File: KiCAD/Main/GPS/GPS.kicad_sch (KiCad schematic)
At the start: 17 parts, among them U1 MAX-M8Q, U2 PHA-23LN

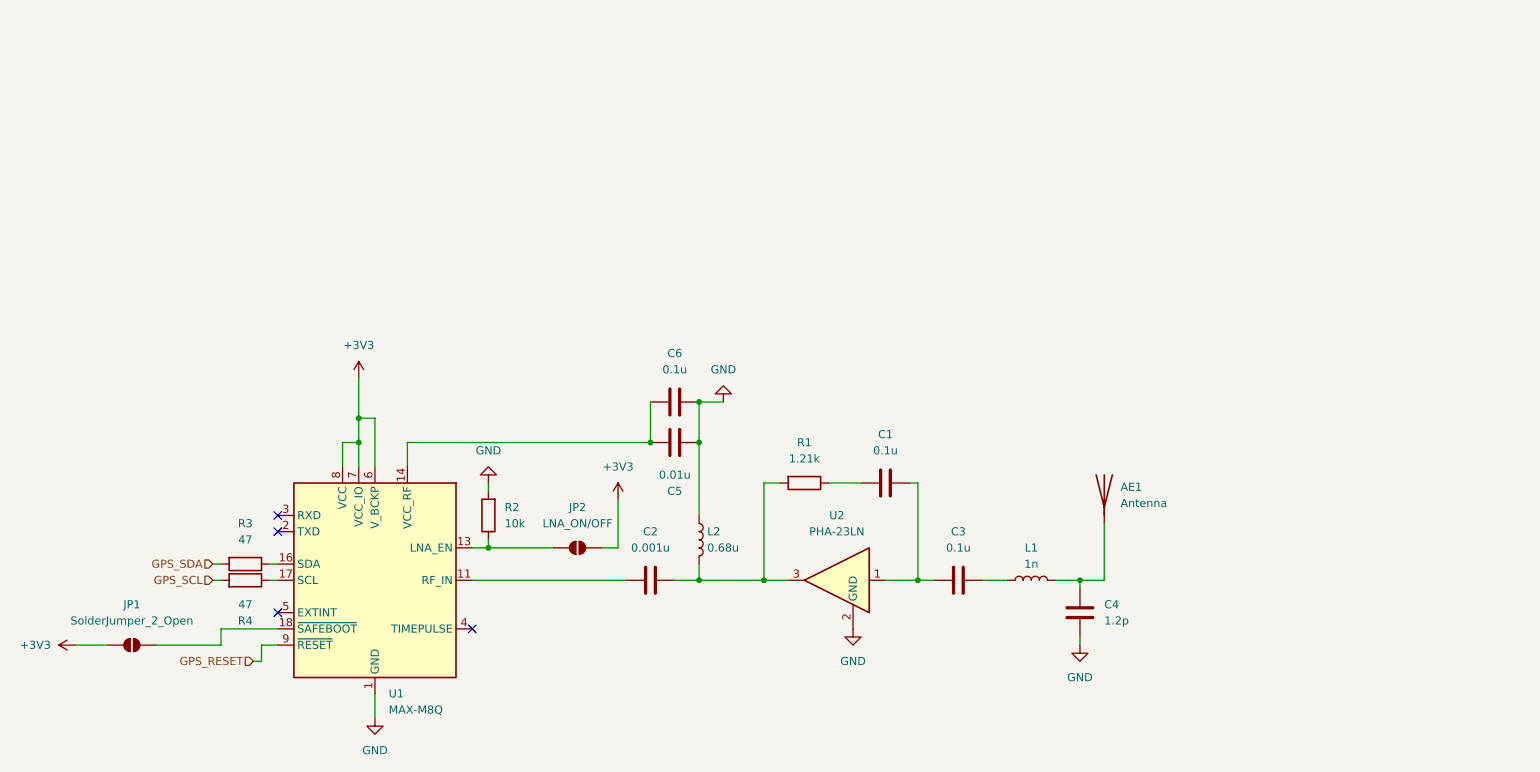
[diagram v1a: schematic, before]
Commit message: Create wiring diagram draft
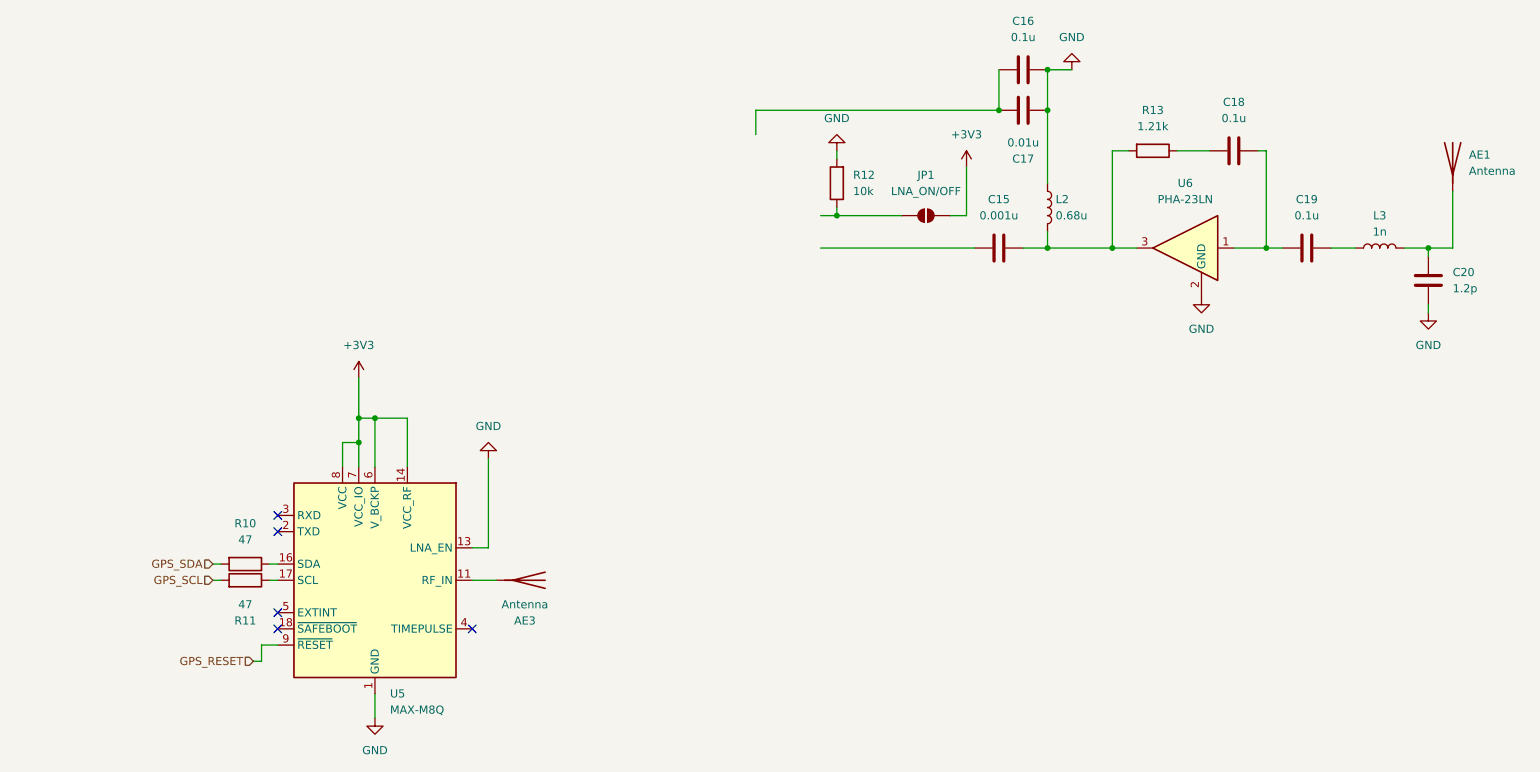
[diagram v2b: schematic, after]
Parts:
- removed JP1: SolderJumper_2_Open, symbol Jumper:SolderJumper_2_Open
- added AE3: Antenna, symbol Device:Antenna
- renumbered C2 to C15, C6 to C16, C5 to C17, C1 to C18, C3 to C19, C4 to C20, JP2 to JP1, L1 to L3, R3 to R10, R4 to R11, R2 to R12, R1 to R13, U1 to U5, U2 to U6
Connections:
- net +3V3: now also U5.14 (VCC_RF)
- net GND: now also U5.13 (LNA_EN)
- net at U5.11 (RF_IN): now also AE3.1 (A); no longer C15.1
- net at JP1.1 (A), R12.1: no longer U5.13 (LNA_EN)
- net at C16.2, C17.2: no longer U5.14 (VCC_RF)
- no-connect marks 4 -> 5
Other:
- moved on the sheet: AE1, C15, C16, C17, C18, C19, C20, JP1, L2, L3, R12, R13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

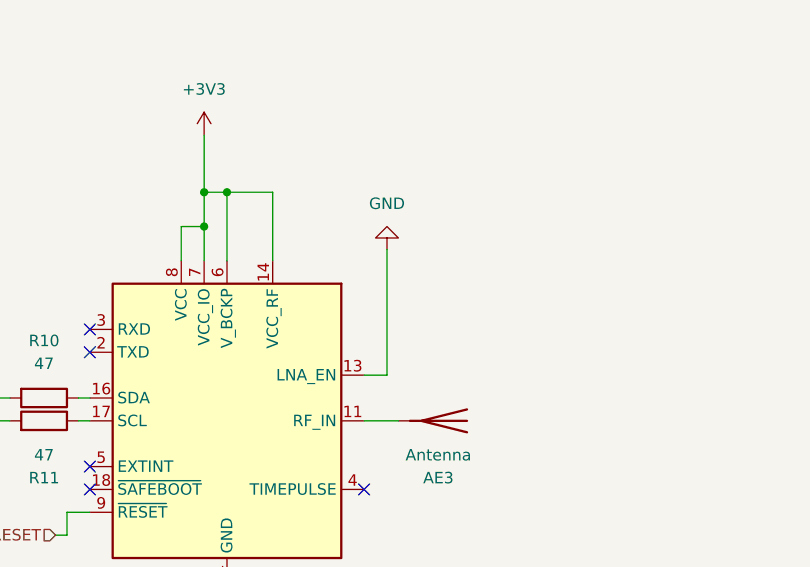
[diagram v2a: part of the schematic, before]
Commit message: Update wiring diagram with TM input
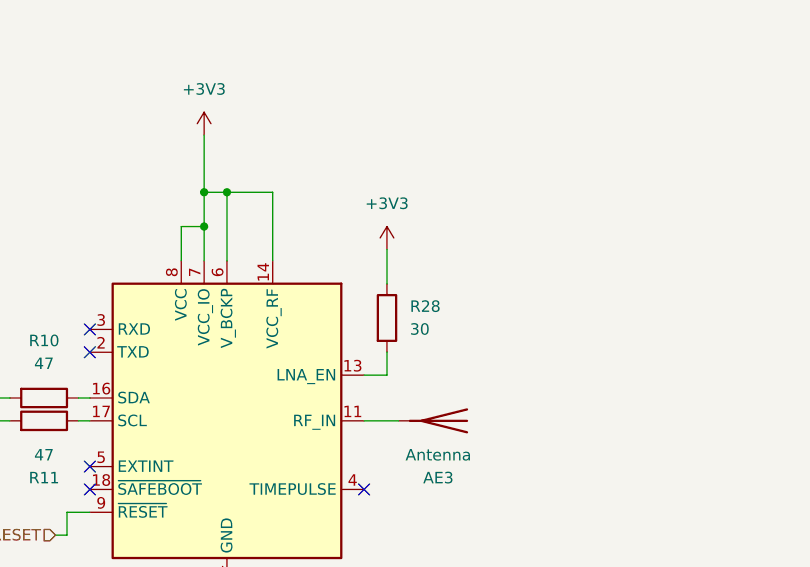
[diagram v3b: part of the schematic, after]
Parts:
- added R28: 30, symbol Device:R
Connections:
- net +3V3: now also R28.1
- net GND: no longer U5.13 (LNA_EN)
- new net: R28.2, U5.13 (LNA_EN)
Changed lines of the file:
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@@
 	(wire
 		(pts
-			(xy 116.84 87.63) (xy 116.84 101.6)
+			(xy 116.84 87.63) (xy 116.84 91.44)
 		)
 		(stroke
@@
 		(pts
 			(xy 82.55 106.68) (xy 83.82 106.68)
+		)
+		(stroke
+			(width 0)
+			(type default)
+		)
+	)
+	(wire
+		(pts
+			(xy 116.84 99.06) (xy 116.84 101.6)
 		)
 		(stroke
@@
 	)
 	(symbol
-		(lib_id "power:GND")
-		(at 116.84 87.63 180)
+		(lib_id "Device:R")
+		(at 116.84 95.25 0)
 		(unit 1)
 		(exclude_from_sim no)
@@
 		(dnp no)
 		(fields_autoplaced yes)
-		(property "Reference" "#PWR018"
-			(at 116.84 81.28 0)
-			(effects
-				(font
-					(size 1.27 1.27)
-				)
-				(hide yes)
-			)
-		)
-		(property "Value" "GND"
-			(at 116.84 82.55 0)
-			(effects
-				(font
-					(size 1.27 1.27)
-				)
-			)
-		)
-		(property "Footprint" ""
-			(at 116.84 87.63 0)
-			(effects
-				(font
-					(size 1.27 1.27)
-				)
-				(hide yes)
-			)
-		)
-		(property "Datasheet" ""
-			(at 116.84 87.63 0)
-			(effects
-				(font
-					(size 1.27 1.27)
-				)
-				(hide yes)
-			)
-		)
-		(property "Description" "Power symbol creates a global label with name \"GND\" , ground"
-			(at 116.84 87.63 0)
-			(effects
-				(font
-					(size 1.27 1.27)
-				)
-				(hide yes)
-			)
-		)
-		(pin "1"
-		)
-		(instances
-			(project "Main"
-				(path "/bbb10697-a5dd-43b8-9c6f-4c5919cf3463/aff6795e-9a09-4ffe-99fb-dba81cca4540"
-					(reference "#PWR018")
+		(property "Reference" "R28"
+			(at 119.38 93.98 0)
+			(effects
+				(font
+					(size 1.27 1.27)
+				)
+				(justify left)
+			)
+		)
+		(property "Value" "30"
+			(at 119.38 96.52 0)
+			(effects
+				(font
+					(size 1.27 1.27)
+				)
+				(justify left)
+			)
+		)
+		(property "Footprint" ""
+			(at 115.062 95.25 90)
+			(effects
+				(font
+					(size 1.27 1.27)
+				)
+				(hide yes)
+			)
+		)
+		(property "Datasheet" "~"
+			(at 116.84 95.25 0)
+			(effects
+				(font
+					(size 1.27 1.27)
+				)
+				(hide yes)
+			)
+		)
+		(property "Description" "Resistor"
+			(at 116.84 95.25 0)
+			(effects
+				(font
+					(size 1.27 1.27)
+				)
+				(hide yes)
+			)
+		)
+		(pin "2"
+		)
+		(pin "1"
+		)
+		(instances
+			(project ""
+				(path "/bbb10697-a5dd-43b8-9c6f-4c5919cf3463/aff6795e-9a09-4ffe-99fb-dba81cca4540"
+					(reference "R28")
 					(unit 1)
 				)
@@
 					(unit 1)
 				)
+			)
+		)
+	)
+	(symbol
+		(lib_id "power:+3V3")
+		(at 116.84 87.63 0)
+		(unit 1)
+		(exclude_from_sim no)
+		(in_bom yes)
+		(on_board yes)
+		(dnp no)
+		(fields_autoplaced yes)
+		(property "Reference" "#PWR018"
+			(at 116.84 91.44 0)
+			(effects
+				(font
+					(size 1.27 1.27)
+				)
+				(hide yes)
+			)
+		)
+		(property "Value" "+3V3"
+			(at 116.84 82.55 0)
+			(effects
+				(font
+					(size 1.27 1.27)
+				)
+			)
+		)
+		(property "Footprint" ""
+			(at 116.84 87.63 0)
+			(effects
+				(font
+					(size 1.27 1.27)
+				)
+				(hide yes)
+			)
+		)
+		(property "Datasheet" ""
+			(at 116.84 87.63 0)
+			(effects
+				(font
+					(size 1.27 1.27)
+				)
+				(hide yes)
+			)
+		)
+		(property "Description" "Power symbol creates a global label with name \"+3V3\""
+			(at 116.84 87.63 0)
+			(effects
+				(font
+					(size 1.27 1.27)
+				)
+				(hide yes)
+			)
+		)
+		(pin "1"
+		)
+		(instances
+			(project ""
+				(path "/bbb10697-a5dd-43b8-9c6f-4c5919cf3463/aff6795e-9a09-4ffe-99fb-dba81cca4540"
+					(reference "#PWR018")
+					(unit 1)
+				)

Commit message: Submit design for review
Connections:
- no-connect marks 5 -> 2
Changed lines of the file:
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@@
-	)
-	(no_connect
-		(at 114.3 114.3)
 	)
 	(no_connect
@@
 	)
 	(no_connect
-		(at 83.82 114.3)
-	)
-	(no_connect
 		(at 83.82 99.06)
 	)
-	(no_connect
-		(at 83.82 111.76)
-	)
 	(wire

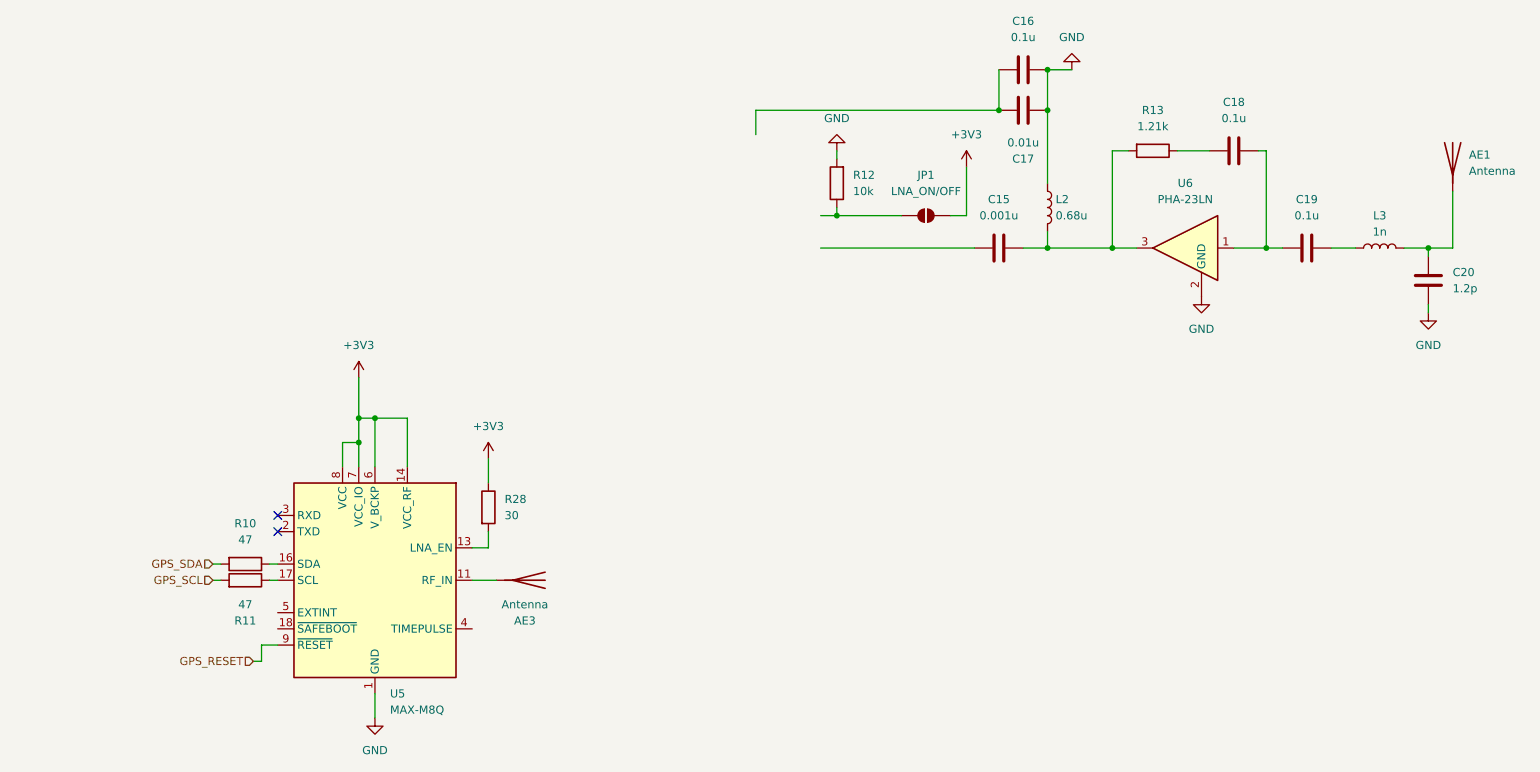
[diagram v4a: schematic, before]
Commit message: Update RF sys and footprints
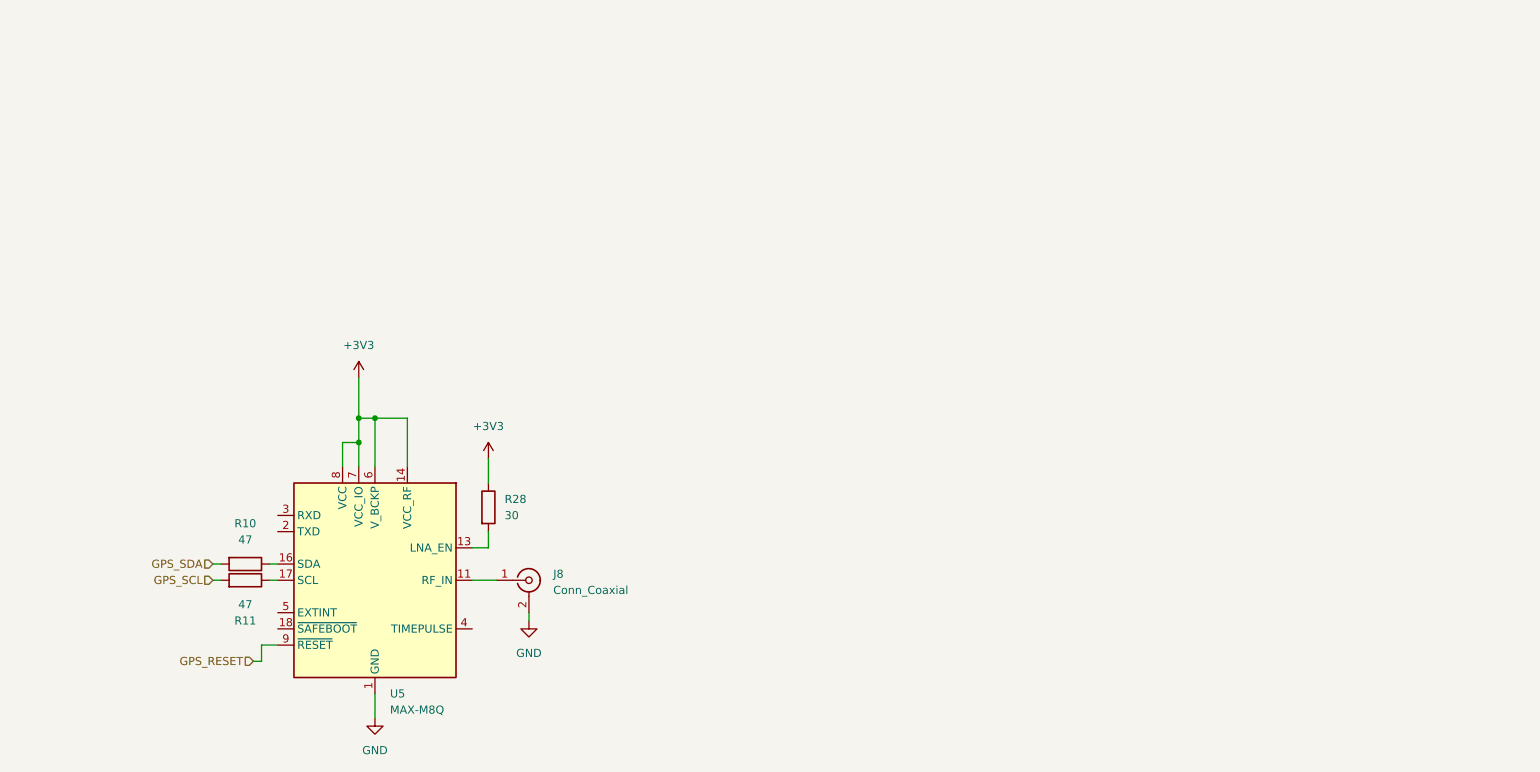
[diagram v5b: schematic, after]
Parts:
- removed AE1, AE3: Antenna, symbol Device:Antenna
- removed C15: 0.001u, symbol Device:C
- removed C16, C18, C19: 0.1u, symbol Device:C
- removed C17: 0.01u, symbol Device:C
- removed C20: 1.2p, symbol Device:C
- removed JP1: LNA_ON/OFF, symbol Jumper:SolderJumper_2_Open
- removed L2: 0.68u, symbol Device:L
- removed L3: 1n, symbol Device:L
- removed R12: 10k, symbol Device:R
- removed R13: 1.21k, symbol Device:R
- removed U6: PHA-23LN, Package_TO_SOT_SMD:SOT-89-3, symbol RF_Amplifier:PHA-23LN
- added J8: Conn_Coaxial, Connector_Coaxial:U.FL_Molex_MCRF_73412-0110_Vertical, symbol Connector:Conn_Coaxial
- R10, R11, R28: footprint (none) -> Resistor_SMD:R_0603_1608Metric
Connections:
- net GND: now also J8.2 (Ext)
- net at U5.11 (RF_IN): now also J8.1 (In)
- no-connect marks 2 -> 0

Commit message: Begin PCB layout
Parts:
- removed R28: 30, Resistor_SMD:R_0603_1608Metric, symbol Device:R
- added C16: 10n, Capacitor_SMD:C_0603_1608Metric, symbol Device:C
- added L2: 47n, symbol Device:L
- added R13: 10, symbol Device:R
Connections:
- net +3V3: now also U5.13 (LNA_EN); no longer U5.14 (VCC_RF)
- net GND: now also C16.2
- net at J8.1 (In), U5.11 (RF_IN): now also L2.2
- new net: C16.1, L2.1, R13.1
- new net: R13.2, U5.14 (VCC_RF)
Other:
- moved on the sheet: J8

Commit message: 30%
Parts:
- L2: footprint (none) -> Inductor_SMD:L_0603_1608Metric
- R13: footprint (none) -> Resistor_SMD:R_0603_1608Metric
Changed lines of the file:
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@@
 			)
 		)
-		(property "Footprint" ""
+		(property "Footprint" "Inductor_SMD:L_0603_1608Metric"
 			(at 125.73 101.6 0)
 			(effects
@@
 			)
 		)
-		(property "Footprint" ""
+		(property "Footprint" "Resistor_SMD:R_0603_1608Metric"
 			(at 127.508 91.44 90)
 			(effects
